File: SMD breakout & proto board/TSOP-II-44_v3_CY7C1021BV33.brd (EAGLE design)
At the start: 25.4 x 27.9 mm, 7 parts

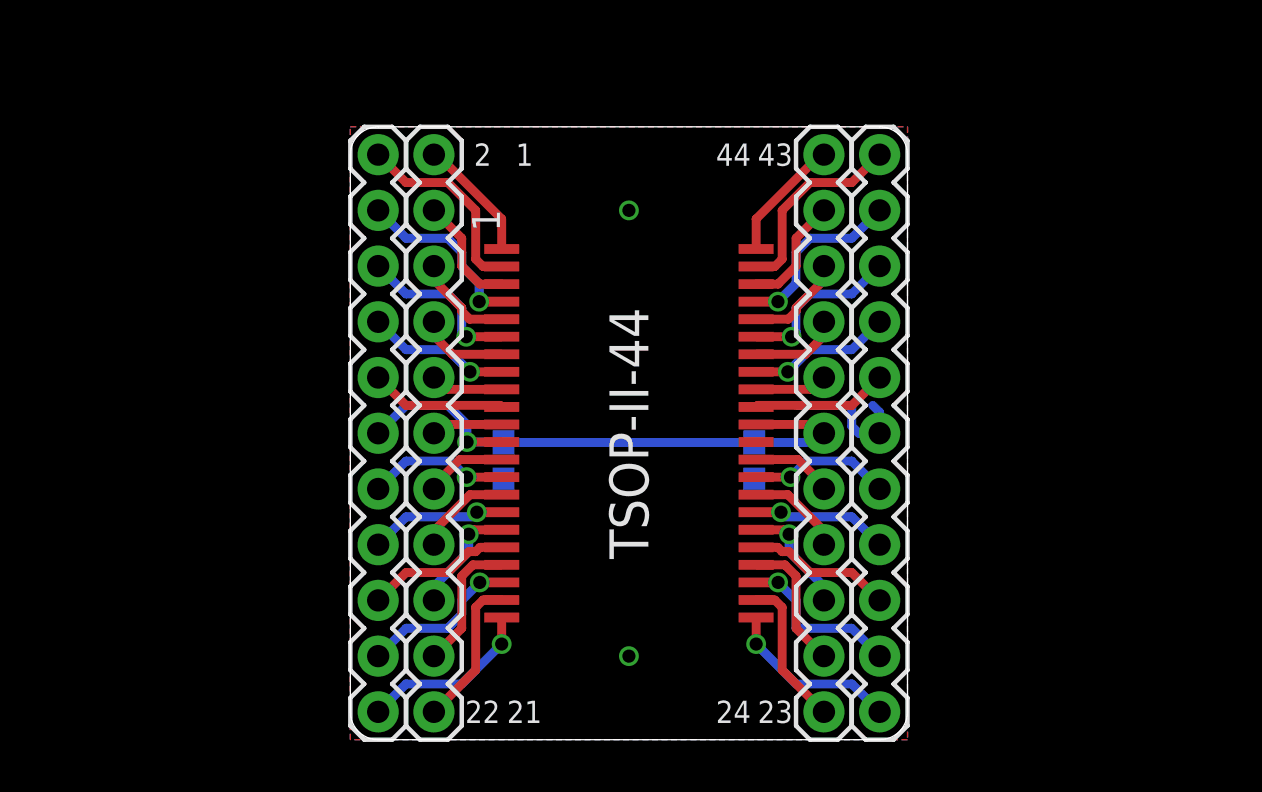
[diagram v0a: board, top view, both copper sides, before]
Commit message: swapped supply pins
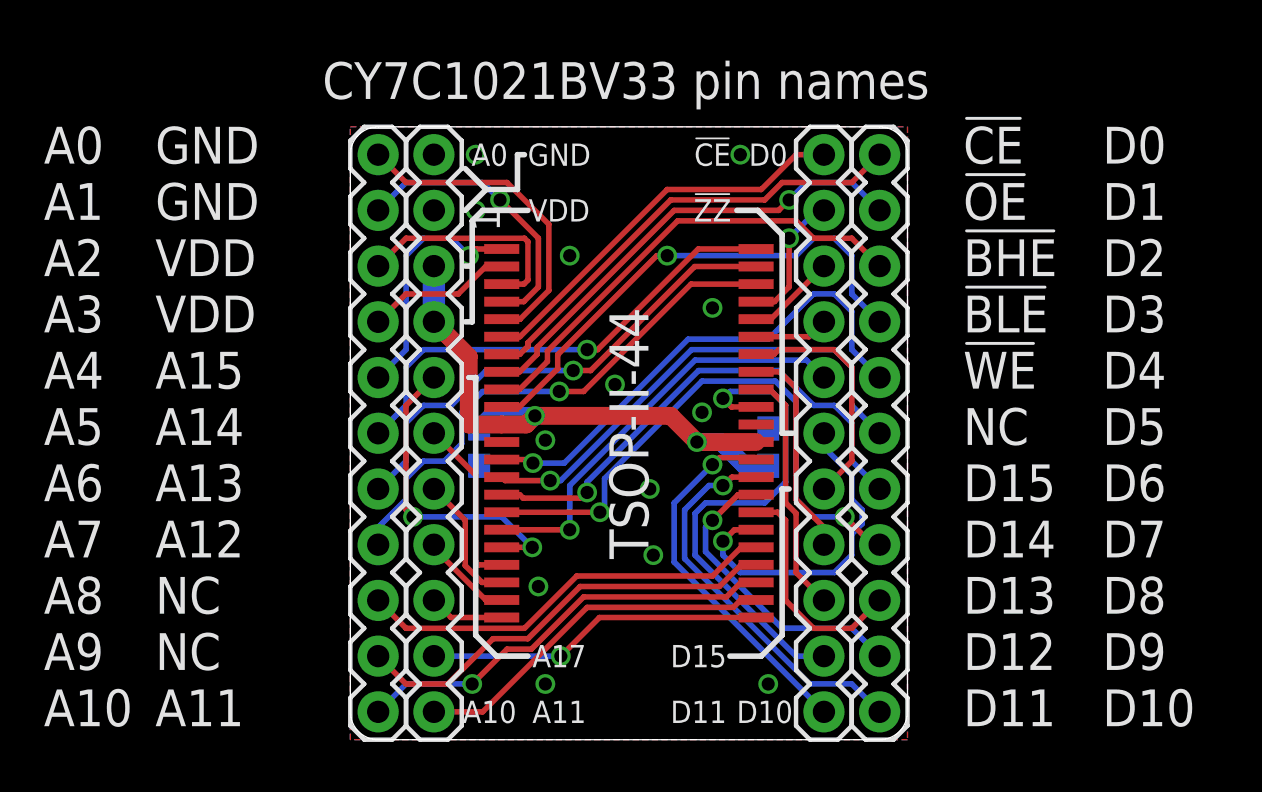
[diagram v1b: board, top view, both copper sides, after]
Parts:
- moved C1 1.28 mm to (5.87, 13.3)
- moved C2 0.90 mm to (19.1, 13.3), turned to 90 degrees
- renumbered JP1 to LEFT_INNER, JP2 to LEFT_OUTER, JP3 to RIGHT_INNER, JP4 to RIGHT_OUTER
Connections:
- net 4 renamed A1
- net 40 renamed !UB
- removed net 1: LEFT_INNER.1, TSOP-II-44.1
- removed net 10: LEFT_OUTER.5, TSOP-II-44.10
- removed net 13: LEFT_INNER.7, TSOP-II-44.13
- removed net 14: LEFT_OUTER.7, TSOP-II-44.14
- removed net 15: LEFT_INNER.8, TSOP-II-44.15
- removed net 16: LEFT_OUTER.8, TSOP-II-44.16
- removed net 17: LEFT_INNER.9, TSOP-II-44.17
- removed net 18: LEFT_OUTER.9, TSOP-II-44.18
- removed net 19: LEFT_INNER.10, TSOP-II-44.19
- removed net 2: LEFT_OUTER.1, TSOP-II-44.2
- removed net 20: LEFT_OUTER.10, TSOP-II-44.20
- removed net 21: LEFT_INNER.11, TSOP-II-44.21
- removed net 22: LEFT_OUTER.11, TSOP-II-44.22
- removed net 23: RIGHT_OUTER.1, TSOP-II-44.23
- removed net 24: RIGHT_INNER.1, TSOP-II-44.24
- removed net 25: RIGHT_OUTER.2, TSOP-II-44.25
- removed net 26: RIGHT_INNER.2, TSOP-II-44.26
- removed net 27: RIGHT_OUTER.3, TSOP-II-44.27
- removed net 28: RIGHT_INNER.3, TSOP-II-44.28
- removed net 29: RIGHT_OUTER.4, TSOP-II-44.29
- removed net 3: LEFT_INNER.2, TSOP-II-44.3
- removed net 30: RIGHT_INNER.4, TSOP-II-44.30
- removed net 31: RIGHT_OUTER.5, TSOP-II-44.31
- removed net 32: RIGHT_INNER.5, TSOP-II-44.32
- removed net 35: RIGHT_OUTER.7, TSOP-II-44.35
- removed net 36: RIGHT_INNER.7, TSOP-II-44.36
- removed net 37: RIGHT_OUTER.8, TSOP-II-44.37
- removed net 38: RIGHT_INNER.8, TSOP-II-44.38
- removed net 39: RIGHT_OUTER.9, TSOP-II-44.39
- removed net 41: RIGHT_OUTER.10, TSOP-II-44.41
- removed net 42: RIGHT_INNER.10, TSOP-II-44.42
- removed net 43: RIGHT_OUTER.11, TSOP-II-44.43
- removed net 44: RIGHT_INNER.11, TSOP-II-44.44
- removed net 5: LEFT_INNER.3, TSOP-II-44.5
- removed net 6: LEFT_OUTER.3, TSOP-II-44.6
- removed net 7: LEFT_INNER.4, TSOP-II-44.7
- removed net 8: LEFT_OUTER.4, TSOP-II-44.8
- removed net 9: LEFT_INNER.5, TSOP-II-44.9
- new net !CE: RIGHT_INNER.11, TSOP-II-44.6
- new net !LB: RIGHT_INNER.8, TSOP-II-44.39
- new net !RD: RIGHT_INNER.10, TSOP-II-44.41
- new net !WR: RIGHT_INNER.7, TSOP-II-44.17
- new net !ZZ: RIGHT_INNER.6, TSOP-II-44.28
- new net A0: LEFT_OUTER.1, TSOP-II-44.5
- new net A10: LEFT_OUTER.11, TSOP-II-44.25
- new net A11: LEFT_INNER.11, TSOP-II-44.24
- new net A12: LEFT_INNER.10, TSOP-II-44.23
- new net A13: LEFT_INNER.9, TSOP-II-44.22
- new net A14: LEFT_INNER.8, TSOP-II-44.21
- new net A15: LEFT_INNER.7, TSOP-II-44.20
- new net A16: LEFT_INNER.6, TSOP-II-44.19
- new net A17: LEFT_INNER.5, TSOP-II-44.18
- new net A2: LEFT_OUTER.3, TSOP-II-44.3
- new net A3: LEFT_OUTER.4, TSOP-II-44.2
- new net A4: LEFT_OUTER.5, TSOP-II-44.1
- new net A5: LEFT_OUTER.6, TSOP-II-44.44
- new net A6: LEFT_OUTER.7, TSOP-II-44.43
- new net A7: LEFT_OUTER.8, TSOP-II-44.42
- new net A8: LEFT_OUTER.9, TSOP-II-44.27
- new net A9: LEFT_OUTER.10, TSOP-II-44.26
- new net D0: RIGHT_OUTER.11, TSOP-II-44.7
- new net D1: RIGHT_OUTER.10, TSOP-II-44.8
- new net D10: RIGHT_OUTER.1, TSOP-II-44.31
- new net D11: RIGHT_INNER.1, TSOP-II-44.32
- new net D12: RIGHT_INNER.2, TSOP-II-44.35
- new net D13: RIGHT_INNER.3, TSOP-II-44.36
- new net D14: RIGHT_INNER.4, TSOP-II-44.37
- new net D15: RIGHT_INNER.5, TSOP-II-44.38
- new net D2: RIGHT_OUTER.9, TSOP-II-44.9
- new net D3: RIGHT_OUTER.8, TSOP-II-44.10
- new net D4: RIGHT_OUTER.7, TSOP-II-44.13
- new net D5: RIGHT_OUTER.6, TSOP-II-44.14
- new net D6: RIGHT_OUTER.5, TSOP-II-44.15
- new net D7: RIGHT_OUTER.4, TSOP-II-44.16
- new net D8: RIGHT_OUTER.3, TSOP-II-44.29
- new net D9: RIGHT_OUTER.2, TSOP-II-44.30
- net GND: now also LEFT_INNER.1, LEFT_INNER.2, TSOP-II-44.12, TSOP-II-44.34; no longer LEFT_INNER.6, RIGHT_OUTER.6, TSOP-II-44.11, TSOP-II-44.33
- net VDD: now also LEFT_INNER.3, LEFT_INNER.4, TSOP-II-44.11, TSOP-II-44.33; no longer LEFT_OUTER.6, RIGHT_INNER.6, TSOP-II-44.12, TSOP-II-44.34
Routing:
- net D7: track 0.00 -> 26.2 mm, vias 0 -> 2
- net A7: track 0.00 -> 24.0 mm, vias 0 -> 1
- net D3: track 0.00 -> 23.4 mm, vias 0 -> 1
- net D6: track 0.00 -> 23.2 mm, vias 0 -> 1
- net D4: track 0.00 -> 23.1 mm, vias 0 -> 1
- net D12: track 0.00 -> 22.8 mm, vias 0 -> 1
- net A6: track 0.00 -> 22.5 mm, vias 0 -> 1
- net D5: track 0.00 -> 22.4 mm, vias 0 -> 1
- net A5: track 0.00 -> 21.7 mm, vias 0 -> 1
- net D2: track 0.00 -> 21.5 mm
- net D1: track 0.00 -> 21.5 mm, vias 0 -> 1
- net D0: track 0.00 -> 21.1 mm
- net A9: track 0.00 -> 20.0 mm
- net A10: track 0.00 -> 19.7 mm, vias 0 -> 1
- net !WR: track 0.00 -> 19.4 mm, vias 0 -> 1
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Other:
- board text added: "!CE"
- board text added: "!CE !OE !BHE !BLE !WE NC D15 D14 D13 D12 D11"
- board text added: "!CE !RD !UB !LB !WR !ZZ D15 D14 D13 D12 D11"
- board text added: "!ZZ"
- board text added: "A0"
- board text added: "A0 A1 A2 A3 A4 A5 A6 A7 A8 A9 A10"
- board text added: "A10"
- board text added: "A11"
- board text added: "A17"
- board text added: "CY7C1021BV33 pin names"
- board text added: "D0"
- board text added: "D0 D1 D2 D3 D4 D5 D6 D7 D8 D9 D10"
- board text added: "D10"
- board text added: "D11"
- board text added: "D15"
- board text added: "GND"
- board text added: "GND GND VDD VDD A15 A14 A13 A12 NC NC A11"
- board text added: "GND GND VDD VDD A17 A16 A15 A14 A13 A12 A11"
- board text added: "VDD"
- board text removed: "1"
- board text removed: "2"
- board text removed: "21"
- board text removed: "22"
- board text removed: "23"
- board text removed: "24"
- board text removed: "43"
- board text removed: "44"
